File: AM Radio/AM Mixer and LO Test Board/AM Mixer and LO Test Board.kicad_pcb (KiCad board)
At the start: 4 copper layers, 100 x 100 mm, 49 parts, among them J1 RF_IN, J2 IF_FILT_OUT, J3 IF_PREFILT_OUT, J4 RF_IN, J5 +12V Input, J6 -12V Input, Q1 2N2222, Q2 2N2222, Q3 2N2222, T1 SWB2010-1-SM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

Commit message: Test Board Routed
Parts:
- moved J6 92.0 mm to (93.3, 53.3)
- moved TP2 79.6 mm to (96.5, 81.3)
- moved C8 77.9 mm to (177.3, 102.1), turned to 270 degrees
- moved L1 75.7 mm to (171.7, 52.3), turned to 270 degrees
- moved TP4 71.6 mm to (96.5, 76.2)
- moved C6 67.9 mm to (158.5, 55.4), turned to 270 degrees
- moved R7 67.7 mm to (159.0, 65.5), turned to 180 degrees
- moved J2 64.9 mm to (106.7, 129.5)
- moved R5 61.9 mm to (162.1, 89.4), turned to 90 degrees
- moved R6 61.8 mm to (165.1, 52.3), turned to 270 degrees
- moved J5 61.2 mm to (187.3, 53.3)
- moved TP1 60.4 mm to (96.5, 86.4)
- moved R3 57.1 mm to (157.5, 89.4), turned to 90 degrees
- moved TP3 55.9 mm to (96.5, 91.4)
- moved Q3 52.5 mm to (150.4, 54.9)
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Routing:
- net Net-(J4-Pad1): track 0.00 -> 122.0 mm, vias 0 -> 2
- net /IF_UNFILT_OUT: track 0.00 -> 114.8 mm
- net Net-(C6-Pad1): track 0.00 -> 58.8 mm, vias 0 -> 2
- net Net-(RV1-Pad2): track 0.00 -> 47.7 mm
- net Net-(FL1-Pad2): track 0.00 -> 35.3 mm
- net Net-(RV1-Pad3): track 0.00 -> 30.7 mm
- net Net-(R8-Pad2): track 0.00 -> 27.7 mm
- net Net-(D3-Pad1): track 0.00 -> 27.6 mm
- net Net-(D3-Pad2): track 0.00 -> 27.3 mm
- net GND: track 0.00 -> 24.4 mm, vias 0 -> 4
- net +12V: track 0.00 -> 23.9 mm, vias 0 -> 1
- net Net-(D4-Pad1): track 0.00 -> 23.6 mm, vias 0 -> 2
- net Net-(Q2-Pad3): track 0.00 -> 22.9 mm, vias 0 -> 2
- net /RF_IN: track 0.00 -> 22.8 mm
- net Net-(C7-Pad2): track 0.00 -> 21.9 mm
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
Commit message: Added power regulation, started work on aligning silk screen.
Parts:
- added C13: 0.1uF, Capacitor_SMD:C_0805_2012Metric_Pad1.15x1.40mm_HandSolder, F.Cu at (182.0, 79.0)
- added C14: 0.1uF, Capacitor_SMD:C_0805_2012Metric_Pad1.15x1.40mm_HandSolder, F.Cu at (184.0, 85.0)
- added D7: 1N4001, Diode_THT:D_DO-15_P15.24mm_Horizontal, F.Cu at (181.0, 73.0)
- added VR1: L7805, Package_TO_SOT_THT:TO-220-3_Vertical, F.Cu at (185.0, 76.0)
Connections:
- U1 pad 5: +12V -> Net-(U1-Pad5)
- U1 pad 7: (no net) -> +12V
- U2 pad 5: +12V -> Net-(U2-Pad5)
- U2 pad 7: (no net) -> +12V
- U3 pad 5: +12V -> Net-(U3-Pad5)
- U3 pad 7: (no net) -> +12V
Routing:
- net +5V: track 0.00 -> 53.6 mm, vias 0 -> 1
- net +12V: track 23.9 -> 76.8 mm
- net GND: track 24.4 -> 33.4 mm
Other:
- board text added: "+12V"
- board text added: "-12V"
- board text added: "GND"

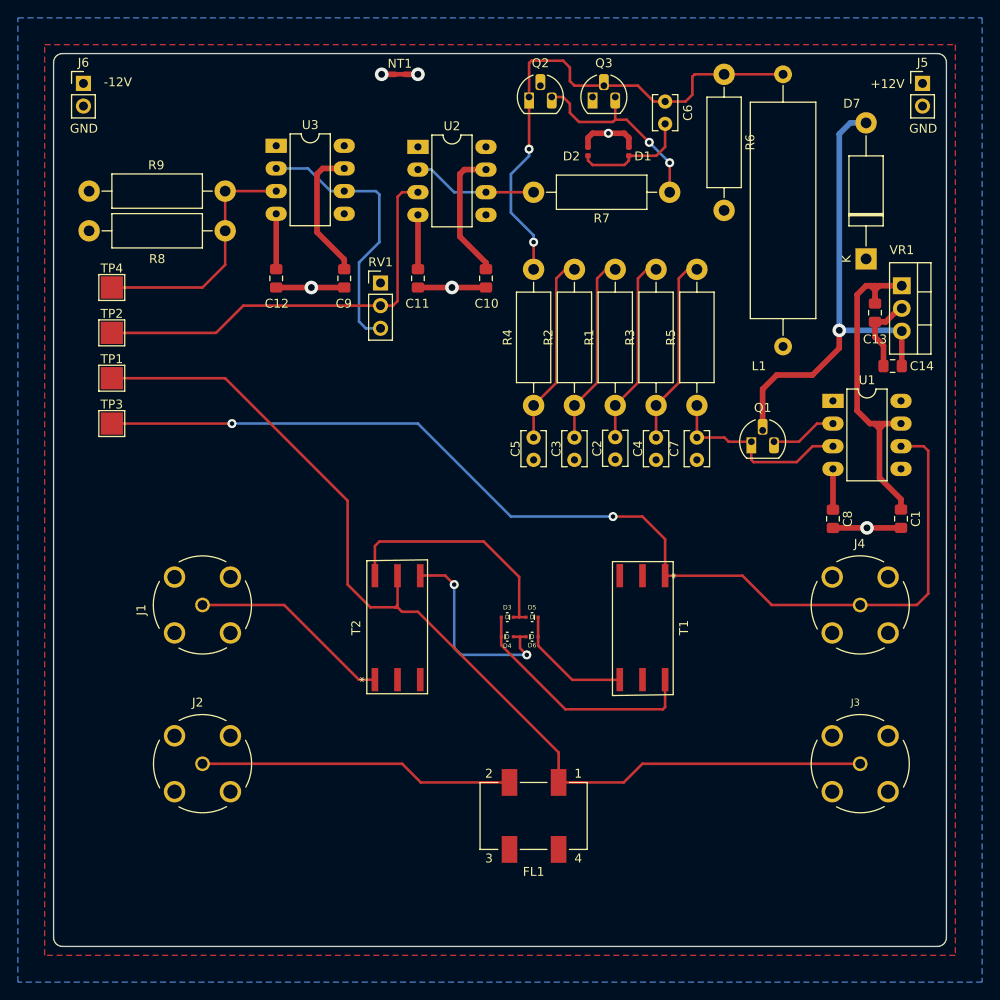
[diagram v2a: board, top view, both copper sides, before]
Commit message: Added extra filter for testing. Finished silk screen editing.
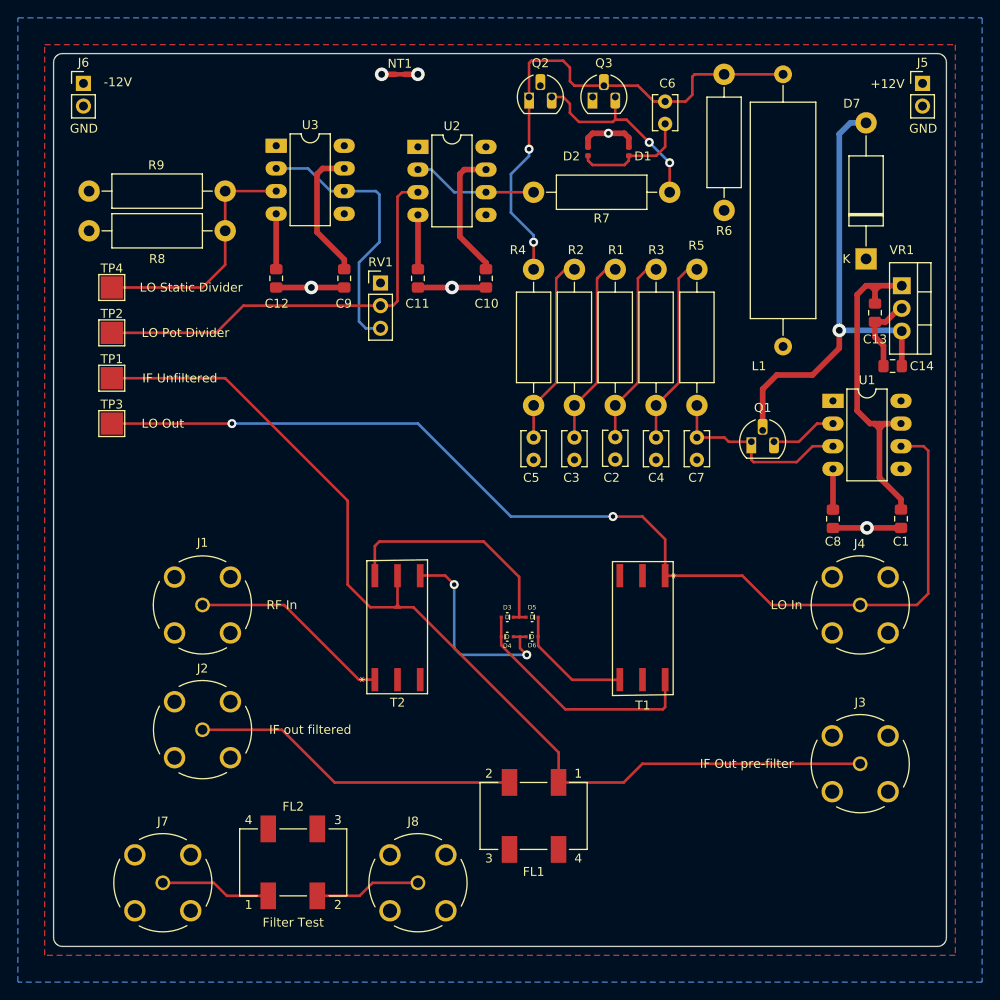
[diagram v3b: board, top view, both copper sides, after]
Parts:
- added FL2: LTC455-W, footprints:LTC455-W, F.Cu at (116.8, 140.3)
- added J7: Filter Test In, footprints:TE_5-1634503-1, F.Cu at (102.2, 142.9)
- added J8: Filter Test Out, footprints:TE_5-1634503-1, F.Cu at (130.8, 142.9)
- J4: value RF_IN -> LO_IN
- moved J2 3.81 mm to (106.7, 125.7)
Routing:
- net Net-(FL2-Pad1): track 0.00 -> 12.4 mm
- net Net-(FL2-Pad2): track 0.00 -> 11.9 mm
- net Net-(FL1-Pad2): track 35.3 -> 36.8 mm
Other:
- board text added: "Filter Test"
- board text added: "IF Out pre-filter"
- board text added: "IF Unfiltered"
- board text added: "IF out filtered"
- board text added: "LO In"
- board text added: "LO Out"
- board text added: "LO Pot Divider"
- board text added: "LO Static Divider"
- board text added: "RF In"

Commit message: Why 12v meme connect to other 12v meme? Grug no know
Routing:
- net +12V: track 76.8 -> 54.7 mm
